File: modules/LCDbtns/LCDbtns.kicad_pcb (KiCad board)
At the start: 2 copper layers, 81.3 x 10.2 mm, 12 parts, among them J1 Conn_01x03_Male, J2 Conn_01x03_Male

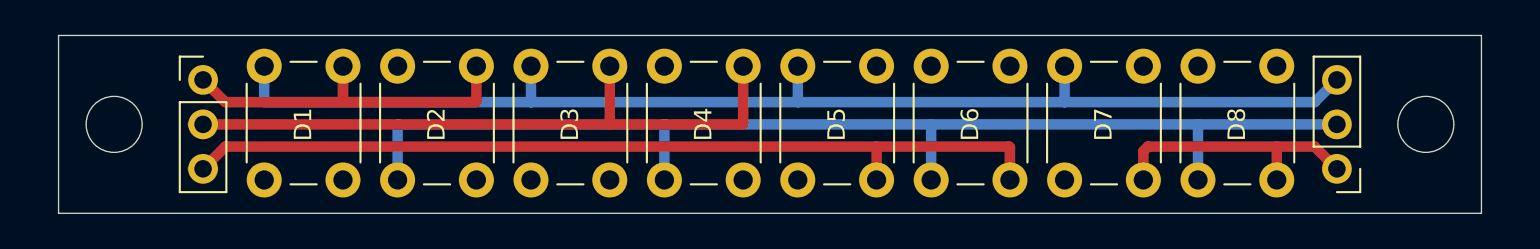
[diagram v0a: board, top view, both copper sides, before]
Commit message: Add diodes to LCD btns PCB. Add gerber.
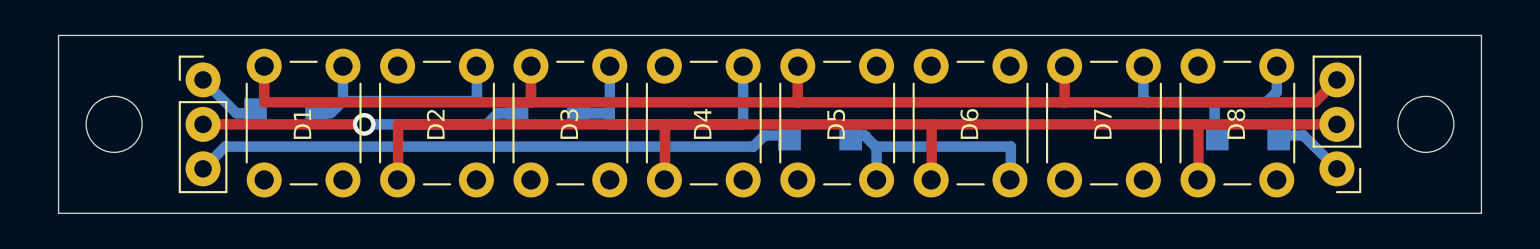
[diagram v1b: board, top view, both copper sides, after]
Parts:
- added VD1: LL4148, Diode_SMD:D_MiniMELF, B.Cu at (89.2, 36.2)
- added VD2: LL4148, Diode_SMD:D_MiniMELF, B.Cu at (104.1, 36.2)
- added VD3: LL4148, Diode_SMD:D_MiniMELF, B.Cu at (119.7, 37.5)
- added VD4: LL4148, Diode_SMD:D_MiniMELF, B.Cu at (144.1, 37.5)
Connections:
- J1 pad 1: Net-(D7-Pad2) -> Net-(J1-Pad1)
- J2 pad 1: Net-(D1-Pad2) -> Net-(J2-Pad1)
- J2 pad 2: Net-(D3-Pad2) -> Net-(J2-Pad2)
- J2 pad 3: Net-(D5-Pad2) -> Net-(J2-Pad3)
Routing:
- net Net-(D3-Pad2): track 57.7 -> 16.0 mm
- net Net-(D5-Pad2): track 51.6 -> 13.2 mm
- net Net-(J2-Pad3): track 0.00 -> 35.5 mm
- net Net-(J2-Pad2): track 0.00 -> 18.2 mm, vias 0 -> 1
- net Net-(D1-Pad2): track 20.2 -> 13.4 mm
- net Net-(J1-Pad1): track 0.00 -> 4.12 mm
- net Net-(J2-Pad1): track 0.00 -> 3.78 mm
- net Net-(D7-Pad2): track 15.2 -> 13.0 mm
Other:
- rule solder_mask_min_width: 0.25 -> 0.1

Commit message: LCD btns. Add pin names.
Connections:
- net Net-(D1-Pad1) renamed /L0
- net Net-(D2-Pad1) renamed /L1
- net Net-(J1-Pad1) renamed /S3
- net Net-(J2-Pad1) renamed /S0
- net Net-(J2-Pad2) renamed /S1
- net Net-(J2-Pad3) renamed /S2

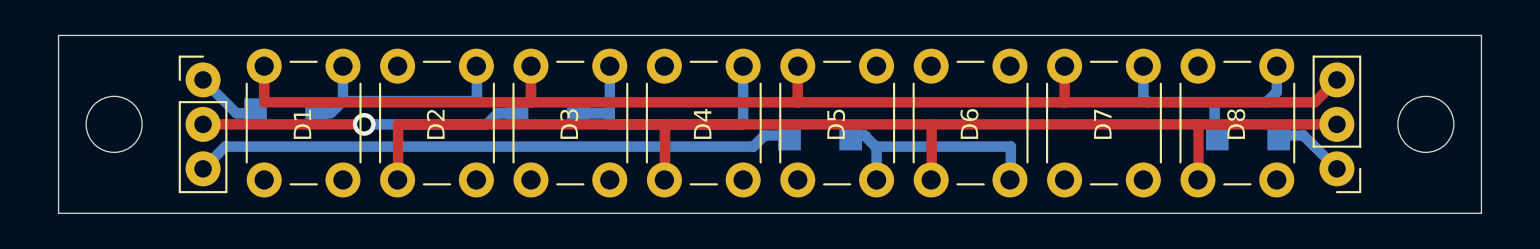
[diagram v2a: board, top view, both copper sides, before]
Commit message: Now 2x shields have distance between 1x parts
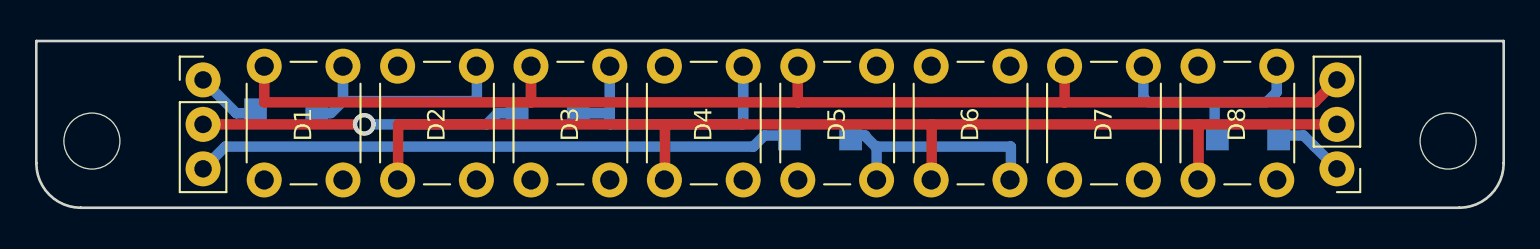
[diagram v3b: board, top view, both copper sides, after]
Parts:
- moved H1 1.59 mm to (78.1, 37.8)
- moved H2 1.59 mm to (155.6, 37.8)
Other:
- board size 81.3 x 10.2 mm -> 83.8 x 9.5 mm

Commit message: Fix hash & version
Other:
- board text added: "b4d799"
- board text added: "v2.3"
